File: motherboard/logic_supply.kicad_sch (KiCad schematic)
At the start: 6 parts, among them U2 M3406-ADJ

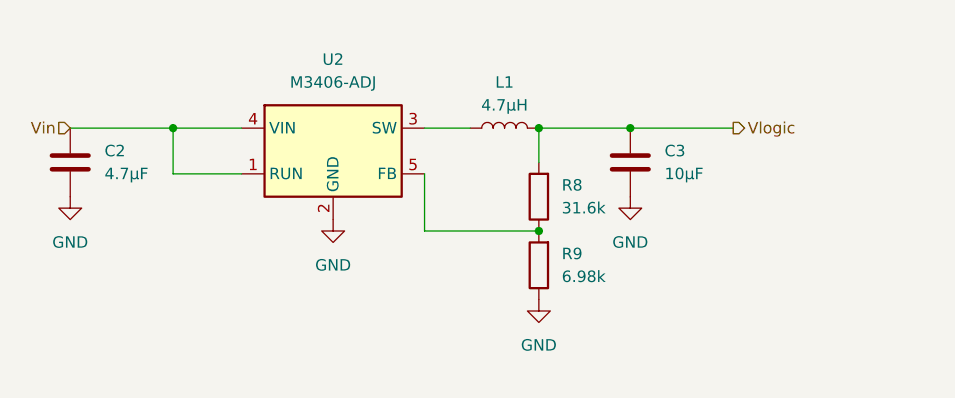
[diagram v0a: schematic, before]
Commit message: reroute motherboard: no traces under antenna
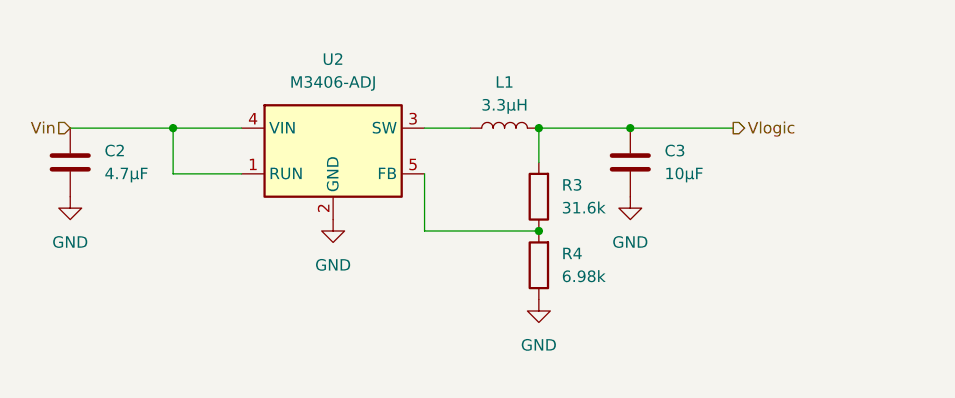
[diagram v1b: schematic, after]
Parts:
- L1: value 4.7µH -> 3.3µH
- renumbered R8 to R3, R9 to R4
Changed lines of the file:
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@@
   (symbol (lib_id "Device:R") (at 110.49 80.01 180) (unit 1)
     (in_bom yes) (on_board yes) (dnp no) (fields_autoplaced)
-    (property "Reference" "R9" (at 113.03 78.74 0)
+    (property "Reference" "R4" (at 113.03 78.74 0)
       (effects (font (size 1.27 1.27)) (justify right))
     )
@@
       (project "motherboard"
         (path "/e63e39d7-6ac0-4ffd-8aa3-1841a4541b55/743fec4a-685a-429b-a3d3-d79ae3ca3a17"
-          (reference "R9") (unit 1)
+          (reference "R4") (unit 1)
         )
       )
@@
       (effects (font (size 1.27 1.27)))
     )
-    (property "Value" "4.7µH" (at 106.68 62.23 90)
+    (property "Value" "3.3µH" (at 106.68 62.23 90)
       (effects (font (size 1.27 1.27)))
     )
@@
   (symbol (lib_id "Device:R") (at 110.49 72.39 180) (unit 1)
     (in_bom yes) (on_board yes) (dnp no) (fields_autoplaced)
-    (property "Reference" "R8" (at 113.03 71.12 0)
+    (property "Reference" "R3" (at 113.03 71.12 0)
       (effects (font (size 1.27 1.27)) (justify right))
     )
@@
       (project "motherboard"
         (path "/e63e39d7-6ac0-4ffd-8aa3-1841a4541b55/743fec4a-685a-429b-a3d3-d79ae3ca3a17"
-          (reference "R8") (unit 1)
+          (reference "R3") (unit 1)
         )
       )

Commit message: motherboard add test points
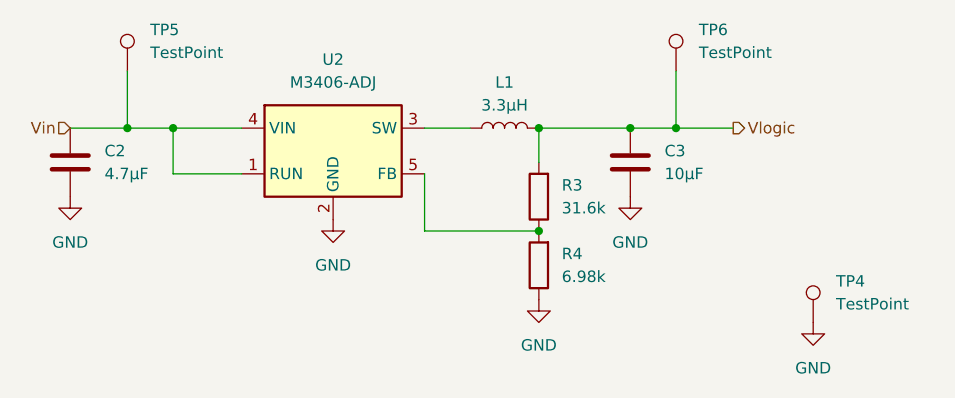
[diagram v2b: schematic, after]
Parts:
- added TP4: TestPoint, TestPoint:TestPoint_THTPad_1.0x1.0mm_Drill0.5mm, symbol Connector:TestPoint
- added TP5, TP6: TestPoint, TestPoint:TestPoint_THTPad_D1.0mm_Drill0.5mm, symbol Connector:TestPoint
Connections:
- net GND: now also TP4.1
- net Vin: now also TP5.1
- net Vlogic: now also TP6.1
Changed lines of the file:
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@@
   (junction (at 110.49 64.77) (diameter 0) (color 0 0 0 0)
   )
+  (junction (at 64.77 64.77) (diameter 0) (color 0 0 0 0)
+  )
+  (junction (at 125.73 64.77) (diameter 0) (color 0 0 0 0)
+  )
   (junction (at 69.85 64.77) (diameter 0) (color 0 0 0 0)
   )
@@
     (stroke (width 0) (type default))
   )
+  (wire (pts (xy 64.77 58.42) (xy 64.77 64.77))
+    (stroke (width 0) (type default))
+  )
   (wire (pts (xy 110.49 64.77) (xy 110.49 68.58))
     (stroke (width 0) (type default))
@@
     (stroke (width 0) (type default))
   )
+  (wire (pts (xy 64.77 64.77) (xy 69.85 64.77))
+    (stroke (width 0) (type default))
+  )
   (wire (pts (xy 69.85 69.85) (xy 69.85 64.77))
     (stroke (width 0) (type default))
   )
-  (wire (pts (xy 120.65 64.77) (xy 132.08 64.77))
+  (wire (pts (xy 120.65 64.77) (xy 125.73 64.77))
+    (stroke (width 0) (type default))
+  )
+  (wire (pts (xy 125.73 58.42) (xy 125.73 64.77))
+    (stroke (width 0) (type default))
+  )
+  (wire (pts (xy 125.73 64.77) (xy 132.08 64.77))
     (stroke (width 0) (type default))
   )
@@
     (stroke (width 0) (type default))
   )
-  (wire (pts (xy 58.42 64.77) (xy 69.85 64.77))
+  (wire (pts (xy 58.42 64.77) (xy 64.77 64.77))
     (stroke (width 0) (type default))
   )
@@
     )
   )
+  (symbol (lib_id "Connector:TestPoint") (at 140.97 86.36 0) (unit 1)
+    (in_bom yes) (on_board yes) (dnp no) (fields_autoplaced)
+    (property "Reference" "TP4" (at 143.51 81.788 0)
+      (effects (font (size 1.27 1.27)) (justify left))
+    )
+    (property "Value" "TestPoint" (at 143.51 84.328 0)
+      (effects (font (size 1.27 1.27)) (justify left))
+    )
+    (property "Footprint" "TestPoint:TestPoint_THTPad_1.0x1.0mm_Drill0.5mm" (at 146.05 86.36 0)
+      (effects (font (size 1.27 1.27)) hide)
+    )
+    (property "Datasheet" "~" (at 146.05 86.36 0)
+      (effects (font (size 1.27 1.27)) hide)
+    )
+    (pin "1")
+    (instances
+      (project "motherboard"
+        (path "/e63e39d7-6ac0-4ffd-8aa3-1841a4541b55"
+          (reference "TP4") (unit 1)
+        )
+        (path "/e63e39d7-6ac0-4ffd-8aa3-1841a4541b55/743fec4a-685a-429b-a3d3-d79ae3ca3a17"
+          (reference "TP5") (unit 1)
+        )
+      )
+    )
+  )
   (symbol (lib_id "power:GND") (at 110.49 83.82 0) (unit 1)
     (in_bom yes) (on_board yes) (dnp no) (fields_autoplaced)
@@
     )
   )
+  (symbol (lib_id "Connector:TestPoint") (at 64.77 58.42 0) (unit 1)
+    (in_bom yes) (on_board yes) (dnp no) (fields_autoplaced)
+    (property "Reference" "TP5" (at 67.31 53.848 0)
+      (effects (font (size 1.27 1.27)) (justify left))
+    )
+    (property "Value" "TestPoint" (at 67.31 56.388 0)
+      (effects (font (size 1.27 1.27)) (justify left))
+    )
+    (property "Footprint" "TestPoint:TestPoint_THTPad_D1.0mm_Drill0.5mm" (at 69.85 58.42 0)
+      (effects (font (size 1.27 1.27)) hide)
+    )
+    (property "Datasheet" "~" (at 69.85 58.42 0)
+      (effects (font (size 1.27 1.27)) hide)
+    )
+    (pin "1")
+    (instances
+      (project "motherboard"
+        (path "/e63e39d7-6ac0-4ffd-8aa3-1841a4541b55"
+          (reference "TP5") (unit 1)
+        )
+        (path "/e63e39d7-6ac0-4ffd-8aa3-1841a4541b55/743fec4a-685a-429b-a3d3-d79ae3ca3a17"
+          (reference "TP4") (unit 1)
+        )
+      )
+    )
+  )
   (symbol (lib_id "power:GND") (at 120.65 72.39 0) (unit 1)
     (in_bom yes) (on_board yes) (dnp no) (fields_autoplaced)
@@
         (path "/e63e39d7-6ac0-4ffd-8aa3-1841a4541b55/743fec4a-685a-429b-a3d3-d79ae3ca3a17"
           (reference "#PWR015") (unit 1)
+        )
+      )
+    )
+  )
+  (symbol (lib_id "Connector:TestPoint") (at 125.73 58.42 0) (unit 1)
+    (in_bom yes) (on_board yes) (dnp no) (fields_autoplaced)
+    (property "Reference" "TP6" (at 128.27 53.848 0)
+      (effects (font (size 1.27 1.27)) (justify left))
+    )
+    (property "Value" "TestPoint" (at 128.27 56.388 0)
+      (effects (font (size 1.27 1.27)) (justify left))
+    )
+    (property "Footprint" "TestPoint:TestPoint_THTPad_D1.0mm_Drill0.5mm" (at 130.81 58.42 0)
+      (effects (font (size 1.27 1.27)) hide)
+    )
+    (property "Datasheet" "~" (at 130.81 58.42 0)
+      (effects (font (size 1.27 1.27)) hide)
+    )
+    (pin "1")
+    (instances
+      (project "motherboard"
+        (path "/e63e39d7-6ac0-4ffd-8aa3-1841a4541b55/743fec4a-685a-429b-a3d3-d79ae3ca3a17"
+          (reference "TP6") (unit 1)
         )
       )
@@
         )
       )
+    )
+  )
+  (symbol (lib_name "GND_3") (lib_id "power:GND") (at 140.97 86.36 0) (unit 1)
+    (in_bom yes) (on_board yes) (dnp no) (fields_autoplaced)
+    (property "Reference" "#PWR033" (at 140.97 92.71 0)
+      (effects (font (size 1.27 1.27)) hide)
+    )
+    (property "Value" "GND" (at 140.97 91.44 0)
+      (effects (font (size 1.27 1.27)))
+    )
+    (property "Footprint" "" (at 140.97 86.36 0)
+      (effects (font (size 1.27 1.27)) hide)
+    )
+    (property "Datasheet" "" (at 140.97 86.36 0)
+      (effects (font (size 1.27 1.27)) hide)
+    )
+    (pin "1")
+    (instances
+      (project "motherboard"
+        (path "/e63e39d7-6ac0-4ffd-8aa3-1841a4541b55"
+          (reference "#PWR033") (unit 1)
+        )
+        (path "/e63e39d7-6ac0-4ffd-8aa3-1841a4541b55/743fec4a-685a-429b-a3d3-d79ae3ca3a17"
+          (reference "#PWR033") (unit 1)
+        )
+      )

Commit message: add 1st order low pass filter, with solder jumper
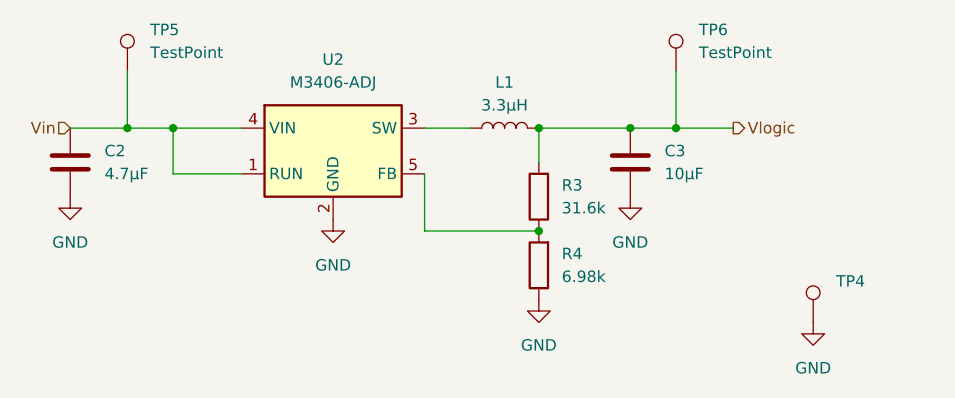
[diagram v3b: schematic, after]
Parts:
- TP4: Label (none) -> GND; now left out of the parts list
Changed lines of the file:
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@@
   )
   (symbol (lib_id "Connector:TestPoint") (at 140.97 86.36 0) (unit 1)
-    (in_bom yes) (on_board yes) (dnp no) (fields_autoplaced)
+    (in_bom no) (on_board yes) (dnp no) (fields_autoplaced)
     (property "Reference" "TP4" (at 143.51 81.788 0)
       (effects (font (size 1.27 1.27)) (justify left))
     )
     (property "Value" "TestPoint" (at 143.51 84.328 0)
-      (effects (font (size 1.27 1.27)) (justify left))
+      (effects (font (size 1.27 1.27)) (justify left) hide)
     )
     (property "Footprint" "TestPoint:TestPoint_THTPad_1.0x1.0mm_Drill0.5mm" (at 146.05 86.36 0)
@@
       (effects (font (size 1.27 1.27)) hide)
     )
+    (property "Label" "GND" (at 140.97 86.36 0)
+      (effects (font (size 1.27 1.27)) (justify left) hide)
+    )
     (pin "1")
